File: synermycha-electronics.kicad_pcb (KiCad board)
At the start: 4 copper layers, 50 x 75 mm, 141 parts, among them J1 BATT, J11 USB_B_Micro, J12 Conn_01x05, J13 Conn_01x05, J14 Conn_01x05, J15 Conn_01x05, J16 Conn_01x05, J17 Conn_01x03, J2 Conn_01x02, J3 Conn_01x02, J4 USB_B_Micro, J5 ESP_01, J6 A1250WV-S-4P, J7 Conn_01x04, J8 Conn_01x04, Q1 IRLML9301TRPBF, Q2 Q_NPN_EBC, Q3 Q_NPN_EBC, Q4 BC847, Q5 Q_NMOS_GDS, Q6 Q_NMOS_GDS, SW1 DTSM32N, SW2 DTSM32N, SW3 DTSM32N, SW4 DTSM32N, U1 LM1117LDX, U12 MPU-9250, U13 STM32F446RETx, U14 STM14_SW, U2 LM1117LDX, U3 LM1117LDX, U4 DRV8835, U8 CP2102N-A01-GQFN28, U9 TS5A3167DBVR, Y1 16MHz, 8pF

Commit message: Added gnd via
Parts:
- Y1: value 16MHz, 8pF -> Crystal_GND24
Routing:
- net GND: vias 35 -> 36
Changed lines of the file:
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@@
     (thickness 1.6)
     (drawings 34)
-    (tracks 1091)
+    (tracks 1092)
     (zones 0)
     (modules 141)
@@
     (add_net "Net-(U14-Pad7)")
   )
+  (module Crystal:Crystal_SMD_Abracon_ABM8G-4Pin_3.2x2.5mm (layer F.Cu)
+    (at 38.3 135.8 180)
+    (descr "Abracon Miniature Ceramic Smd Crystal ABM8G http://www.abracon.com/Resonators/ABM8G.pdf, 3.2x2.5mm^2 package")
+    (tags "SMD SMT crystal")
+    (attr smd)
+    (fp_text reference Y1 (at 0 -2.45) (layer F.SilkS)
+      (effects (font (size 1 1) (thickness 0.15)))
+    )
+    (fp_text value Crystal_GND24 (at 0 2.45) (layer F.Fab)
+      (effects (font (size 1 1) (thickness 0.15)))
+    )
+    (fp_text user %R (at 0 0) (layer F.Fab)
+      (effects (font (size 0.7 0.7) (thickness 0.105)))
+    )
+    (fp_line (start -1.4 -1.25) (end 1.4 -1.25) (layer F.Fab) (width 0.1))
+    (fp_line (start 1.4 -1.25) (end 1.6 -1.05) (layer F.Fab) (width 0.1))
+    (fp_line (start 1.6 -1.05) (end 1.6 1.05) (layer F.Fab) (width 0.1))
+    (fp_line (start 1.6 1.05) (end 1.4 1.25) (layer F.Fab) (width 0.1))
+    (fp_line (start 1.4 1.25) (end -1.4 1.25) (layer F.Fab) (width 0.1))
+    (fp_line (start -1.4 1.25) (end -1.6 1.05) (layer F.Fab) (width 0.1))
+    (fp_line (start -1.6 1.05) (end -1.6 -1.05) (layer F.Fab) (width 0.1))
+    (fp_line (start -1.6 -1.05) (end -1.4 -1.25) (layer F.Fab) (width 0.1))
+    (fp_line (start -1.6 0.25) (end -0.6 1.25) (layer F.Fab) (width 0.1))
+    (fp_line (start -2 -1.65) (end -2 1.65) (layer F.SilkS) (width 0.12))
+    (fp_line (start -2 1.65) (end 2 1.65) (layer F.SilkS) (width 0.12))
+    (fp_line (start -2.1 -1.7) (end -2.1 1.7) (layer F.CrtYd) (width 0.05))
+    (fp_line (start -2.1 1.7) (end 2.1 1.7) (layer F.CrtYd) (width 0.05))
+    (fp_line (start 2.1 1.7) (end 2.1 -1.7) (layer F.CrtYd) (width 0.05))
+    (fp_line (start 2.1 -1.7) (end -2.1 -1.7) (layer F.CrtYd) (width 0.05))
+    (pad 1 smd rect (at -1.1 0.85 180) (size 1.4 1.2) (layers F.Cu F.Paste F.Mask)
+      (net 44 "Net-(C30-Pad1)"))
+    (pad 2 smd rect (at 1.1 0.85 180) (size 1.4 1.2) (layers F.Cu F.Paste F.Mask)
+      (net 1 GND))
+    (pad 3 smd rect (at 1.1 -0.85 180) (size 1.4 1.2) (layers F.Cu F.Paste F.Mask)
+      (net 45 "Net-(C31-Pad2)"))
+    (pad 4 smd rect (at -1.1 -0.85 180) (size 1.4 1.2) (layers F.Cu F.Paste F.Mask)
+      (net 1 GND))
+    (model ${KISYS3DMOD}/Crystal.3dshapes/Crystal_SMD_Abracon_ABM8G-4Pin_3.2x2.5mm.wrl
+      (at (xyz 0 0 0))
+      (scale (xyz 1 1 1))
+      (rotate (xyz 0 0 0))
+    )
+  )
   (module Connector_JST:JST_GH_BM04B-GHS-TBT_1x04-1MP_P1.25mm_Vertical (layer F.Cu)
     (at 50.4 153.5 180)
@@
     )
   )
-  (module Crystal:Crystal_SMD_Abracon_ABM8G-4Pin_3.2x2.5mm (layer F.Cu)
-    (at 38.289 135.809 180)
-    (descr "Abracon Miniature Ceramic Smd Crystal ABM8G http://www.abracon.com/Resonators/ABM8G.pdf, 3.2x2.5mm^2 package")
-    (tags "SMD SMT crystal")
-    (attr smd)
-    (fp_text reference Y1 (at 0 2.5) (layer Dwgs.User) hide
-      (effects (font (size 1 1) (thickness 0.15)))
-    )
-    (fp_text value "16MHz, 8pF" (at 0 2.45) (layer F.Fab)
-      (effects (font (size 1 1) (thickness 0.15)))
-    )
-    (fp_line (start 2.1 -1.7) (end -2.1 -1.7) (layer F.CrtYd) (width 0.05))
-    (fp_line (start 2.1 1.7) (end 2.1 -1.7) (layer F.CrtYd) (width 0.05))
-    (fp_line (start -2.1 1.7) (end 2.1 1.7) (layer F.CrtYd) (width 0.05))
-    (fp_line (start -2.1 -1.7) (end -2.1 1.7) (layer F.CrtYd) (width 0.05))
-    (fp_line (start -2 1.65) (end 2 1.65) (layer F.SilkS) (width 0.12))
-    (fp_line (start -2 -1.65) (end -2 1.65) (layer F.SilkS) (width 0.12))
-    (fp_line (start -1.6 0.25) (end -0.6 1.25) (layer F.Fab) (width 0.1))
-    (fp_line (start -1.6 -1.05) (end -1.4 -1.25) (layer F.Fab) (width 0.1))
-    (fp_line (start -1.6 1.05) (end -1.6 -1.05) (layer F.Fab) (width 0.1))
-    (fp_line (start -1.4 1.25) (end -1.6 1.05) (layer F.Fab) (width 0.1))
-    (fp_line (start 1.4 1.25) (end -1.4 1.25) (layer F.Fab) (width 0.1))
-    (fp_line (start 1.6 1.05) (end 1.4 1.25) (layer F.Fab) (width 0.1))
-    (fp_line (start 1.6 -1.05) (end 1.6 1.05) (layer F.Fab) (width 0.1))
-    (fp_line (start 1.4 -1.25) (end 1.6 -1.05) (layer F.Fab) (width 0.1))
-    (fp_line (start -1.4 -1.25) (end 1.4 -1.25) (layer F.Fab) (width 0.1))
-    (fp_text user %R (at 0 0) (layer F.Fab) hide
-      (effects (font (size 0.7 0.7) (thickness 0.105)))
-    )
-    (pad 4 smd rect (at -1.1 -0.85 180) (size 1.4 1.2) (layers F.Cu F.Paste F.Mask)
-      (net 1 GND))
-    (pad 3 smd rect (at 1.1 -0.85 180) (size 1.4 1.2) (layers F.Cu F.Paste F.Mask)
-      (net 45 "Net-(C31-Pad2)"))
-    (pad 2 smd rect (at 1.1 0.85 180) (size 1.4 1.2) (layers F.Cu F.Paste F.Mask)
-      (net 1 GND))
-    (pad 1 smd rect (at -1.1 0.85 180) (size 1.4 1.2) (layers F.Cu F.Paste F.Mask)
-      (net 44 "Net-(C30-Pad1)"))
-    (model ${KISYS3DMOD}/Crystal.3dshapes/Crystal_SMD_Abracon_ABM8G-4Pin_3.2x2.5mm.wrl
-      (at (xyz 0 0 0))
-      (scale (xyz 1 1 1))
-      (rotate (xyz 0 0 0))
-    )
-  )
   (module Connector_USB:USB_Micro-B_Amphenol_10103594-0001LF_Horizontal (layer F.Cu)
     (at 46 195)
@@
   (via (at 55.118 155.702) (size 0.6) (drill 0.3) (layers F.Cu B.Cu) (net 1))
   (via (at 55.118 154.94) (size 0.6) (drill 0.3) (layers F.Cu B.Cu) (net 1))
+  (via (at 35.7 137) (size 0.8) (drill 0.4) (layers F.Cu B.Cu) (net 1))
   (segment (start 49.1 185.6) (end 49.5 186) (width 0.3048) (layer F.Cu) (net 2))
   (segment (start 49.1 184.1) (end 49.1 185.6) (width 0.3048) (layer F.Cu) (net 2))

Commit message: Applied changes to PCB
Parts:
- removed J7, J8: Conn_01x04, Connector_PinHeader_1.00mm:PinHeader_1x04_P1.00mm_Vertical_SMD_Pin1Left
- added C20: 10uF, Capacitor_SMD:C_0603_1608Metric, F.Cu at (52.5, 187.0)
- added C21: 1uF, Capacitor_SMD:C_0402_1005Metric, F.Cu at (52.2, 184.5)
- added D22: WS2812B, WS2812-2020:WS28122020, B.Cu at (37.0, 196.5)
- added D23: RED, LED_SMD:LED_0402_1005Metric, B.Cu at (27.8, 137.8)
- added D24: RED, LED_SMD:LED_0402_1005Metric, F.Cu at (33.5, 129.5)
- added R27: 330, Resistor_SMD:R_0402_1005Metric, F.Cu at (30.8, 138.2)
- added R28: 330, Resistor_SMD:R_0402_1005Metric, F.Cu at (33.5, 131.5)
- added REF**: mocowanie_silników, mocowanie_silników:mocowanie_silników, F.Cu at (36.9, 168.5)
- added REF**: MountingHole_2.2mm_M2, MountingHole:MountingHole_2.2mm_M2, F.Cu at (47.9, 181.2)
- added REF**: MountingHole_2.2mm_M2, MountingHole:MountingHole_2.2mm_M2, F.Cu at (26.1, 181.2)
- added REF**: MountingHole_2.2mm_M2, MountingHole:MountingHole_2.2mm_M2, F.Cu at (47.9, 157.8)
- added REF**: MountingHole_2.2mm_M2, MountingHole:MountingHole_2.2mm_M2, F.Cu at (26.1, 157.8)
- added REF**: hole_0.8mm, holes:hole_0.8mm, F.Cu at (27.8, 137.8)
- added U5: LM1117LDX, Package_SON:WSON-8_4x4mm_P0.8mm, F.Cu at (49.5, 186.0)
- D6: footprint LED_SMD:LED_0603_1608Metric -> LED_SMD:LED_0402_1005Metric; moved to F.Cu
- Y1: value Crystal_GND24 -> 16Mhz, 8pF
- moved G*** 36.9 mm to (28.5, 146.5), turned to 90 degrees
- moved R11 29.6 mm to (22.6, 153.2), turned to 180 degrees
- moved R30 28.5 mm to (22.6, 152.1), turned to 180 degrees
- moved J6 28.3 mm to (22.5, 148.5), turned to 0 degrees
- moved D1 24.8 mm to (48.3, 134.6), turned to 225 degrees
- moved D6 22.7 mm to (41.0, 129.5)
- moved BZ1 20.9 mm to (46.5, 131.5), turned to 225 degrees
- moved R26 18.8 mm to (41.0, 131.5), turned to 270 degrees
- moved R21 17.2 mm to (46.5, 135.6), turned to 315 degrees
- moved Q4 15.8 mm to (44.5, 135.5), turned to 45 degrees
- moved C3 14.1 mm to (40.1, 180.2)
- moved C6 14.1 mm to (39.9, 177.7)
- moved U1 14.1 mm to (37.1, 179.2)
- moved R4 13.7 mm to (34.6, 180.7)
- moved R3 13.7 mm to (34.6, 178.7)
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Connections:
- D10 pad 1: +3V3 -> +5V
- D11 pad 1: +3V3 -> +5V
- D12 pad 1: +3V3 -> +5V
- D13 pad 1: +3V3 -> +5V
- D13 pad 2: (no net) -> Net-(D13-Pad2)
- D2 pad 2: (no net) -> /LED & Oled & Buzzer/~LED_1
- D20 pad 1: +3V3 -> +5V
- D21 pad 1: +3V3 -> +5V
- D3 pad 2: (no net) -> /LED & Oled & Buzzer/~LED_2
- D4 pad 2: (no net) -> /LED & Oled & Buzzer/~LED_3
- D5 pad 2: (no net) -> /LED & Oled & Buzzer/~LED_4
- D6 pad 2: (no net) -> /LED & Oled & Buzzer/~LED_5
- D7 pad 1: +3V3 -> +5V
- D8 pad 1: +3V3 -> +5V
- D9 pad 1: +3V3 -> +5V
- U13 pad 10: (no net) -> /LED & Oled & Buzzer/~LED_2
- U13 pad 11: (no net) -> /LED & Oled & Buzzer/~LED_1
- U13 pad 14: (no net) -> /LED & Oled & Buzzer/~LED_6
- U13 pad 16: (no net) -> Net-(D18-Pad2)
- U13 pad 2: (no net) -> Net-(D19-Pad2)
- U13 pad 20: (no net) -> /LED & Oled & Buzzer/~LED_MOUSE_EYE
- U13 pad 21: (no net) -> Net-(D17-Pad2)
- U13 pad 3: (no net) -> Net-(D15-Pad2)
- U13 pad 4: (no net) -> /LED & Oled & Buzzer/~LED_5
- U13 pad 50: (no net) -> /Buttons/~BUTTON_UP
- U13 pad 51: (no net) -> /Buttons/~BUTTON_OK
- U13 pad 52: (no net) -> /Buttons/~BUTTON_DOWN
- U13 pad 54: (no net) -> Net-(D16-Pad2)
- U13 pad 8: (no net) -> /LED & Oled & Buzzer/~LED_4
- U13 pad 9: (no net) -> /LED & Oled & Buzzer/~LED_3
- U4 pad 2: Net-(J2-Pad1) -> Net-(J2-Pad2)
- U4 pad 3: Net-(J2-Pad2) -> Net-(J2-Pad1)
- U4 pad 4: Net-(J3-Pad1) -> Net-(J3-Pad2)
- U4 pad 5: Net-(J3-Pad2) -> Net-(J3-Pad1)
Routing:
- net +5V: track 0.00 -> 251.6 mm, vias 0 -> 12
- net +3V3: track 473.8 -> 331.3 mm, vias 12 -> 5
- net /uController/STM32_D-: track 1.55 -> 54.7 mm, vias 1 -> 2
- net /uController/STM32_D+: track 1.89 -> 55.0 mm, vias 1 -> 2
- net Net-(D13-Pad2): track 0.00 -> 28.3 mm, vias 0 -> 2
- net Net-(D19-Pad2): track 1.13 -> 23.2 mm, vias 0 -> 2
- net Net-(D17-Pad2): track 1.02 -> 21.6 mm, vias 0 -> 2
- net /LED & Oled & Buzzer/~LED_1: track 0.00 -> 19.9 mm, vias 0 -> 2
- net /LED & Oled & Buzzer/~LED_6: track 0.00 -> 19.7 mm, vias 0 -> 2
- net Net-(D16-Pad2): track 1.02 -> 19.9 mm, vias 0 -> 2
- net /LED & Oled & Buzzer/~LED_3: track 0.00 -> 17.9 mm, vias 0 -> 2
- net /LED & Oled & Buzzer/~LED_4: track 0.00 -> 17.3 mm, vias 0 -> 2
- net +6V: track 42.8 -> 25.5 mm
- net /LED & Oled & Buzzer/~LED_2: track 0.00 -> 17.0 mm, vias 0 -> 2
- net /Buttons/~BUTTON_DOWN: track 54.0 -> 70.3 mm, vias 2 -> 3
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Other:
- rule via_min_size: 0.6 -> 0.4

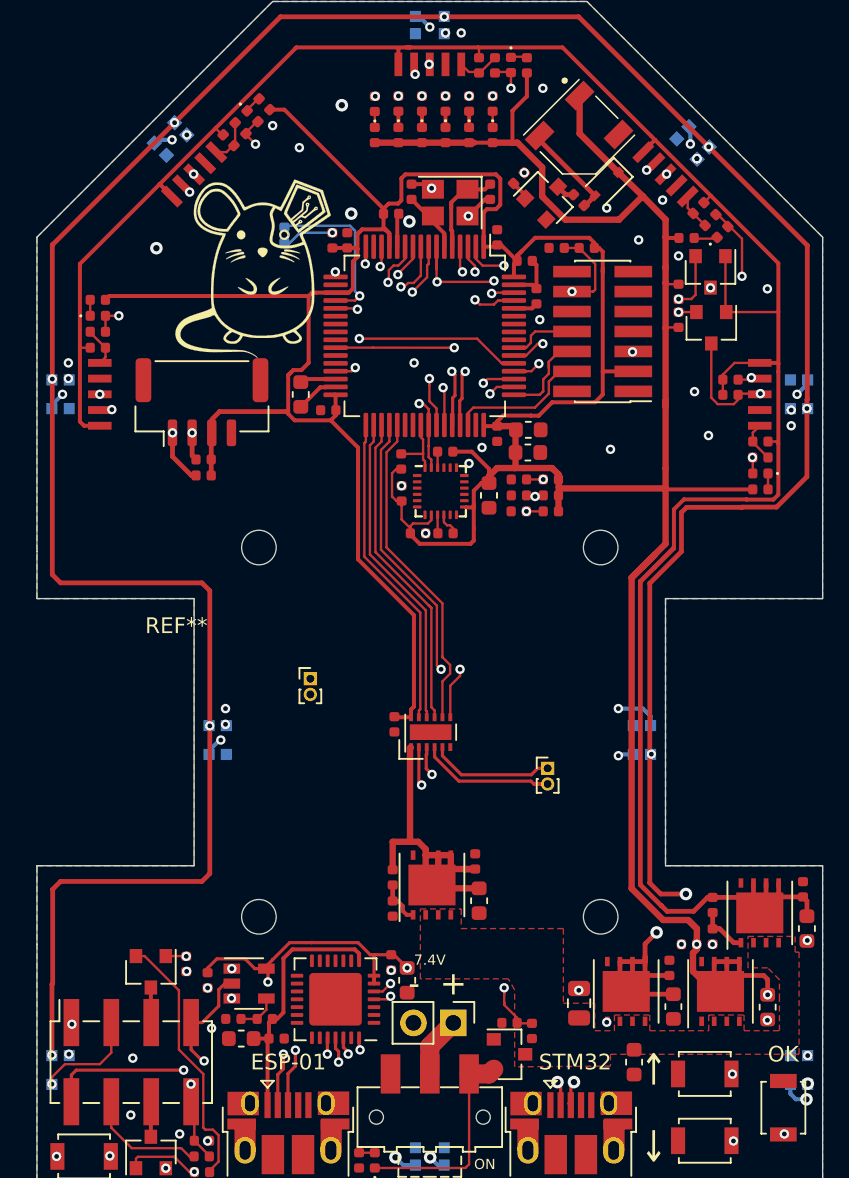
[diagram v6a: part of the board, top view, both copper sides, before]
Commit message: Added connection to RGB for STM32, remapped some pins
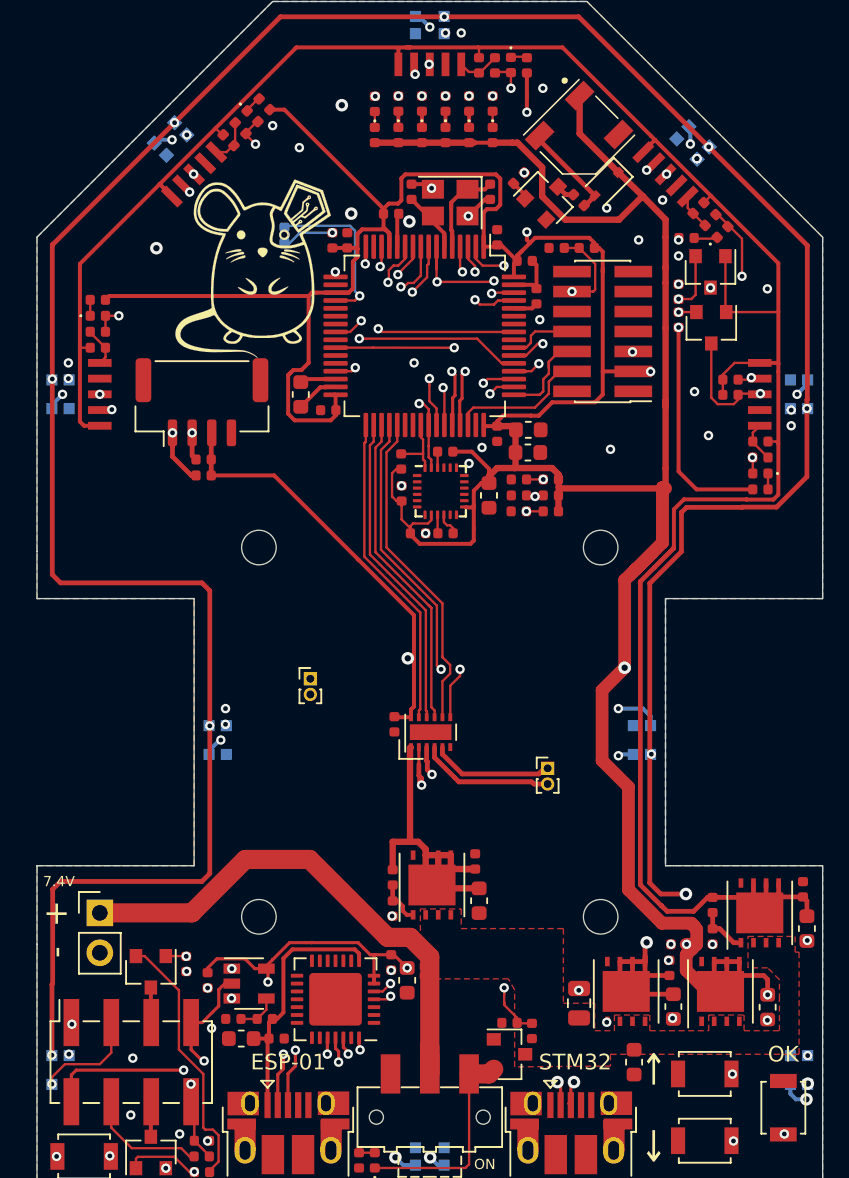
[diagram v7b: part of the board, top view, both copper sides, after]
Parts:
- removed the REF** at (36.9, 168.5)
- moved J1 23.6 mm to (16.0, 181.0), turned to 0 degrees
- moved C7 0.67 mm to (52.8, 183.0)
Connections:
- U13 pad 21: Net-(D17-Pad2) -> (no net)
- U13 pad 24: (no net) -> Net-(D17-Pad2)
- U13 pad 57: (no net) -> /RGB/WS2812B_IN
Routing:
- net /RGB/WS2812B_IN: track 6.78 -> 104.3 mm, vias 1 -> 2
- net +3V3: track 331.3 -> 383.9 mm, vias 5 -> 13
- net Net-(J1-Pad1): track 3.87 -> 34.2 mm
- net Net-(J2-Pad1): track 13.4 -> 24.6 mm
- net Net-(J3-Pad2): track 9.27 -> 17.8 mm
- net Net-(D17-Pad2): track 21.6 -> 19.4 mm
- net Net-(J2-Pad2): track 13.6 -> 14.9 mm
- net GND: vias 43 -> 46

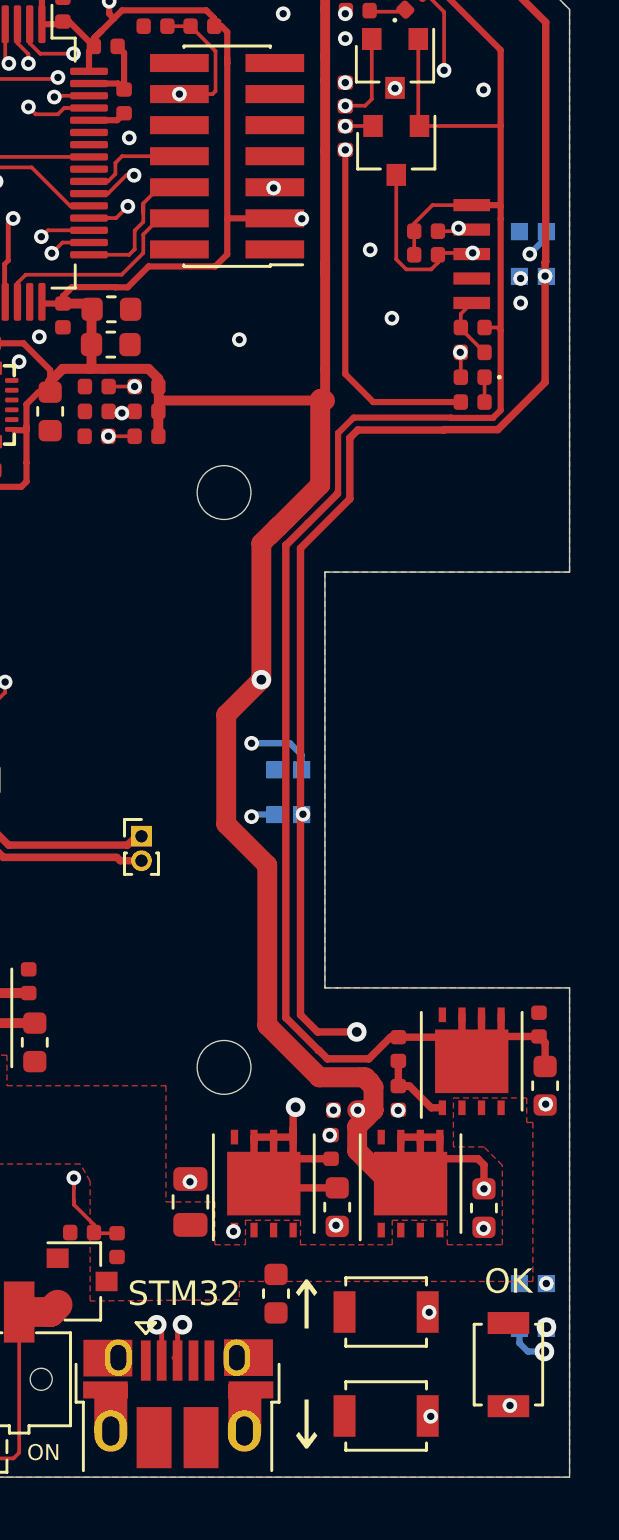
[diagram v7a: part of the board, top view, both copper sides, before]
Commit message: Minor changes in pinout and layout
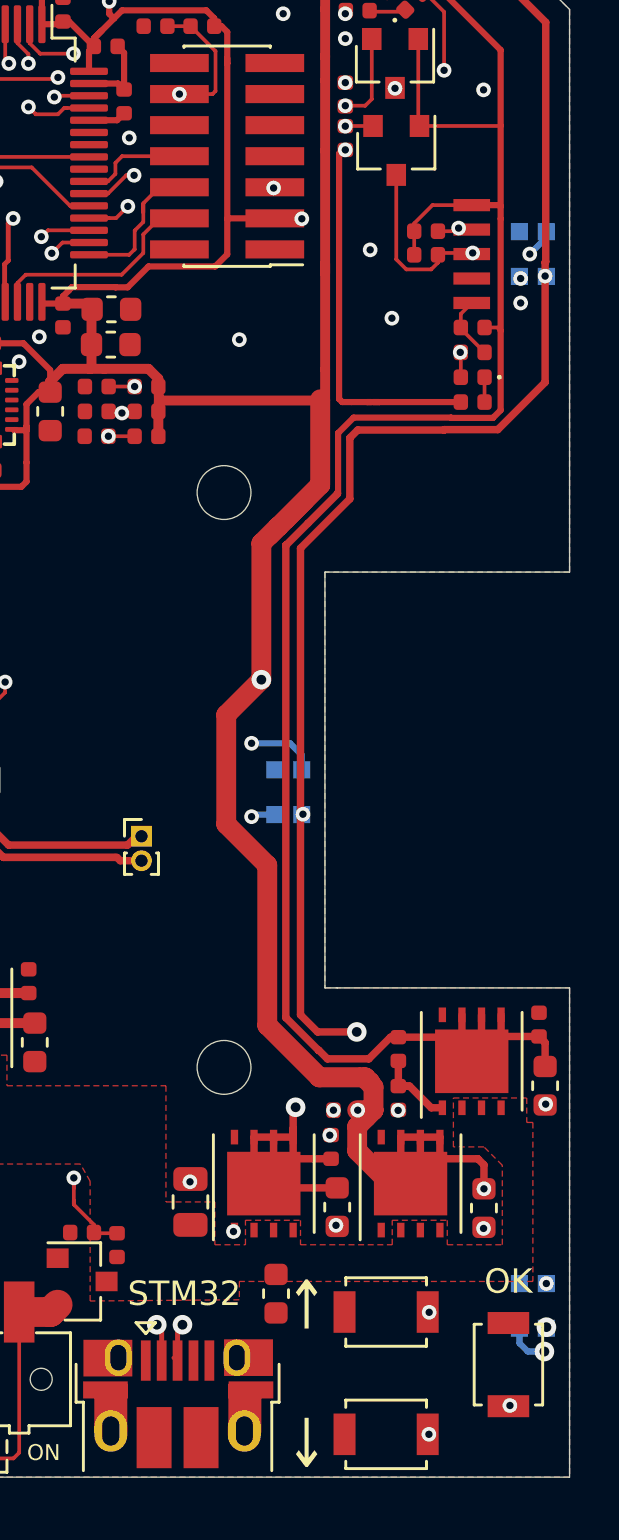
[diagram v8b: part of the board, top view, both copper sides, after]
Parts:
- moved SW3 0.75 mm to (54.5, 196.2)
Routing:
- net +3V3: track 383.9 -> 385.1 mm
